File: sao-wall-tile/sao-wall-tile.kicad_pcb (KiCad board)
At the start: 2 copper layers, 100 x 86.5 mm, 22 parts, among them J1 Power In, J2 Power Out, J3 Power Out, J4 Conn_02x03_Odd_Even, J5 Conn_02x03_Odd_Even, J6 Conn_02x03_Odd_Even, J7 Conn_02x03_Odd_Even, U1 LM2594M-3.3

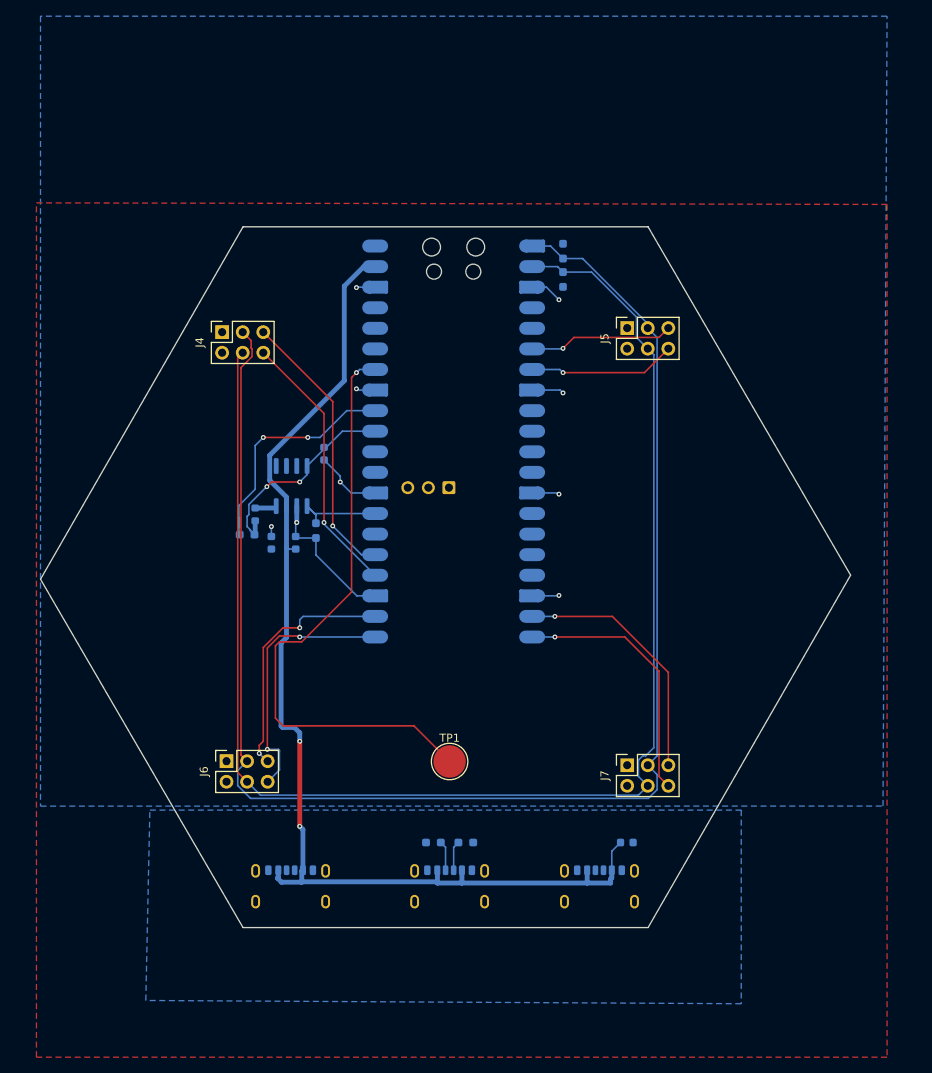
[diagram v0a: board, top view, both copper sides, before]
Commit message: Add README, clean up schematic and layout
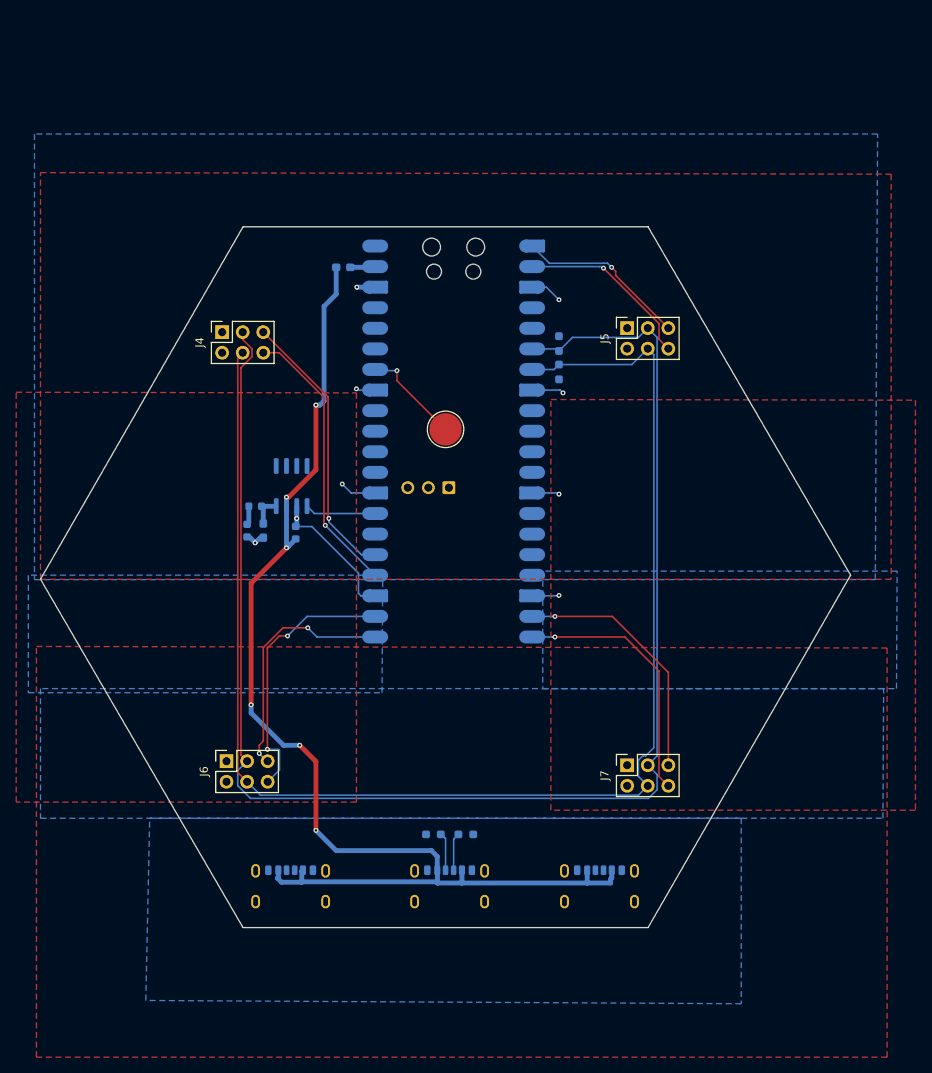
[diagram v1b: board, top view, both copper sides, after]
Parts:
- removed C3: 68uF, Capacitor_SMD:C_0603_1608Metric
- removed C4: 120uF, Capacitor_SMD:C_0603_1608Metric
- removed NT1: NetTie_2, NetTie:NetTie-2_SMD_Pad0.5mm
- removed R1: 1M, Resistor_SMD:R_0603_1608Metric_Pad0.98x0.95mm_HandSolder
- removed R4: 10, Resistor_SMD:R_0603_1608Metric_Pad0.98x0.95mm_HandSolder
- added D1: D_Schottky, Diode_SMD:D_0603_1608Metric_Pad1.05x0.95mm_HandSolder, B.Cu at (102.5, 87.5)
- added D2: D_Schottky, Diode_SMD:D_0603_1608Metric_Pad1.05x0.95mm_HandSolder, B.Cu at (112.4, 55.0)
- C1: value 10uF -> 68uF
- C2: value C -> 120uF
- moved C1 56.0 mm to (106.5, 87.8), turned to 90 degrees
- moved TP1 41.0 mm to (125.0, 75.0)
- moved R2 11.4 mm to (139.0, 64.4)
- moved R3 11.4 mm to (139.0, 67.9)
- moved C2 3.35 mm to (100.5, 87.5), turned to -90 degrees
- moved L1 1.00 mm to (101.5, 84.5), turned to 180 degrees
- moved R7 1.00 mm to (127.5, 125.0)
- moved R8 1.00 mm to (123.5, 125.0)
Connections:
- A1 pad 1: /SAO_SDA -> /SAO2_GPIO1
- A1 pad 2: /SAO_SCL -> /SAO2_GPIO2
- A1 pad 21: /SAO3_GPIO2 -> /SAO3_GPIO1
- A1 pad 22: /SAO3_GPIO1 -> /SAO3_GPIO2
- A1 pad 31: /3V3_HI -> unconnected-(A1-GPIO26_ADC0-Pad31)
- A1 pad 32: /3V3_LO -> unconnected-(A1-GPIO27_ADC1-Pad32)
- A1 pad 39: +5V -> Net-(A1-VSYS)
- A1 pad 6: /SAO2_GPIO1 -> /SAO_SDA
- A1 pad 7: /SAO2_GPIO2 -> /SAO_SCL
- L1 pad 2: /3V3_HI -> +3V3
- U1 pad 4: /3V3_HI -> +3V3
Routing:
- net /TOUCH: track 74.6 -> 12.5 mm
- net /3V3_LO: track 26.4 -> 0.00 mm, vias 2 -> 0
- net /3V3_HI: track 26.1 -> 0.00 mm, vias 2 -> 0
- net +5V: track 139.6 -> 148.8 mm, vias 2 -> 6
- net /SAO_SCL: track 180.0 -> 175.4 mm
- net /SAO2_GPIO2: track 18.2 -> 22.7 mm
- net /SAO2_GPIO1: track 17.9 -> 21.3 mm
- net GND: track 46.8 -> 43.4 mm
- net /SAO_SDA: track 187.9 -> 184.6 mm
- net Net-(A1-VSYS): track 0.00 -> 3.10 mm
- net /EN_3V3: track 11.4 -> 8.78 mm
- net Net-(D1-K): track 2.69 -> 4.03 mm
- net +3V3: track 1.04 -> 2.31 mm
- net /SAO1_GPIO2: track 33.2 -> 34.3 mm
- net Net-(J1-CC2): track 3.71 -> 4.76 mm
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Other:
- board text added: "Power In USB 5V"
- board text added: "Power Out 5V"

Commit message: Update from review feedback
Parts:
- C1, C2: footprint Capacitor_SMD:C_0603_1608Metric -> Capacitor_SMD:C_0805_2012Metric_Pad1.18x1.45mm_HandSolder
- D1, D2: footprint Diode_SMD:D_0603_1608Metric_Pad1.05x0.95mm_HandSolder -> Diode_SMD:D_0805_2012Metric_Pad1.15x1.40mm_HandSolder
- L1: footprint Inductor_SMD:L_0603_1608Metric -> Inductor_SMD:L_0805_2012Metric_Pad1.05x1.20mm_HandSolder
- R2, R3, R7, R8: footprint Resistor_SMD:R_0603_1608Metric_Pad0.98x0.95mm_HandSolder -> Resistor_SMD:R_0805_2012Metric_Pad1.20x1.40mm_HandSolder
- moved D2 1.88 mm to (110.5, 55.0)
- moved R2 1.85 mm to (140.8, 65.0), turned to 180 degrees
- moved R3 1.76 mm to (140.8, 67.8), turned to 180 degrees
- moved C2 1.12 mm to (99.5, 88.0)
- moved C1 1.03 mm to (106.2, 88.8), turned to 0 degrees
- moved A1 1.00 mm to (125.0, 76.5)
- moved R7 0.75 mm to (128.2, 125.0)
- moved R8 0.75 mm to (122.8, 125.0)
- moved D1 0.56 mm to (102.2, 88.0)
- moved L1 0.25 mm to (101.2, 84.5)
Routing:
- net +3V3: track 2.31 -> 191.2 mm, vias 0 -> 1
- net GND: track 43.4 -> 7.90 mm, vias 9 -> 3
- net +5V: track 148.8 -> 137.4 mm, vias 6 -> 0
- net /SAO4_GPIO2: track 32.0 -> 36.3 mm
- net /SAO_SCL: track 175.4 -> 179.7 mm
- net /SAO4_GPIO1: track 31.1 -> 33.9 mm
- net /SAO1_GPIO2: track 34.3 -> 36.1 mm
- net /SAO_SDA: track 184.6 -> 186.1 mm
- net /TOUCH: track 12.5 -> 13.5 mm
- net Net-(A1-VSYS): track 3.10 -> 4.10 mm
- net /EN_3V3: track 8.78 -> 7.78 mm
- net /SAO1_GPIO1: track 34.2 -> 35.1 mm
- net Net-(J1-CC2): track 4.76 -> 5.67 mm
- net Net-(J1-CC1): track 4.71 -> 5.37 mm
- net /SAO2_GPIO2: track 22.7 -> 22.1 mm, vias 1 -> 0
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- removed copper zone on B.Cu, net +3V3
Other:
- board text added: "GPIO1 SDA 3v3 GPIO2 SCL GND"
- board text added: "SAO Wall Tile"
- board text added: "https://github.com/bwasserm/sao-wall v1.0"

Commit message: Updates from picking components on digikey
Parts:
- C1: footprint Capacitor_SMD:C_0805_2012Metric_Pad1.18x1.45mm_HandSolder -> Capacitor_SMD:C_Elec_5x5.8
- C2: footprint Capacitor_SMD:C_0805_2012Metric_Pad1.18x1.45mm_HandSolder -> Capacitor_SMD:C_Elec_8x10.2
- D1: footprint Diode_SMD:D_0805_2012Metric_Pad1.15x1.40mm_HandSolder -> Diode_SMD:D_SOD-123
- L1: value 100uH -> 47uH; footprint Inductor_SMD:L_0805_2012Metric_Pad1.05x1.20mm_HandSolder -> Inductor_SMD:L_Taiyo-Yuden_NR-60xx_HandSoldering
- moved C2 5.37 mm to (95.8, 91.8)
- moved L1 4.37 mm to (99.5, 80.5), turned to 90 degrees
- moved C1 1.68 mm to (107.8, 89.5)
- moved D1 0.50 mm to (101.8, 88.0)
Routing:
- net GND: track 7.90 -> 0.00 mm, vias 3 -> 12
- net Net-(D1-K): track 4.35 -> 9.90 mm
- net +3V3: track 191.2 -> 193.3 mm
- net /SAO1_GPIO1: track 35.1 -> 34.2 mm
- net /SAO1_GPIO2: track 36.1 -> 35.4 mm

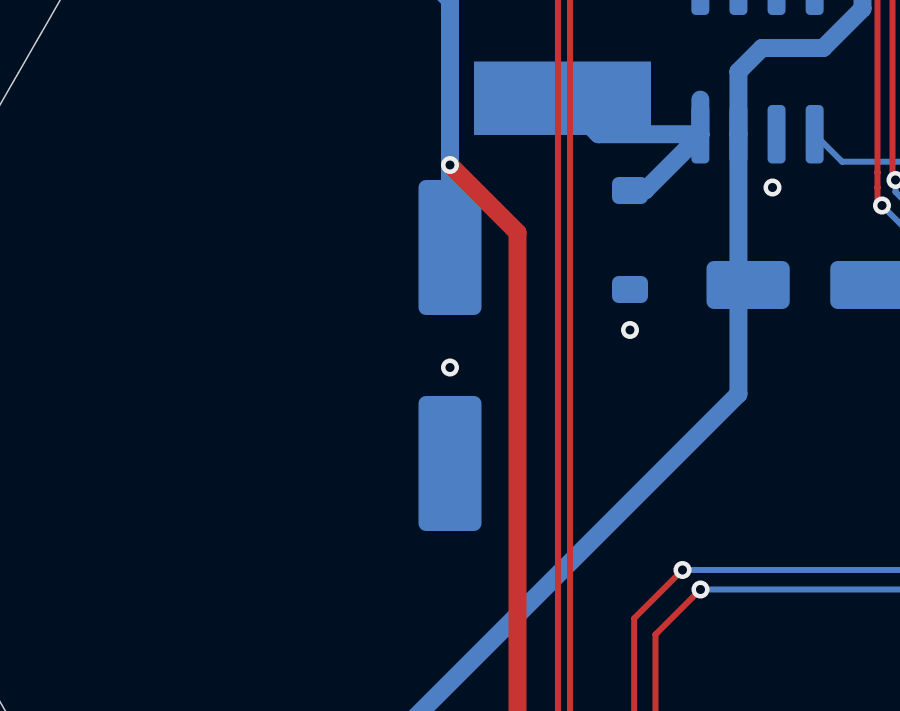
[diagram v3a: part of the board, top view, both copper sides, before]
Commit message: Made C2 smaller
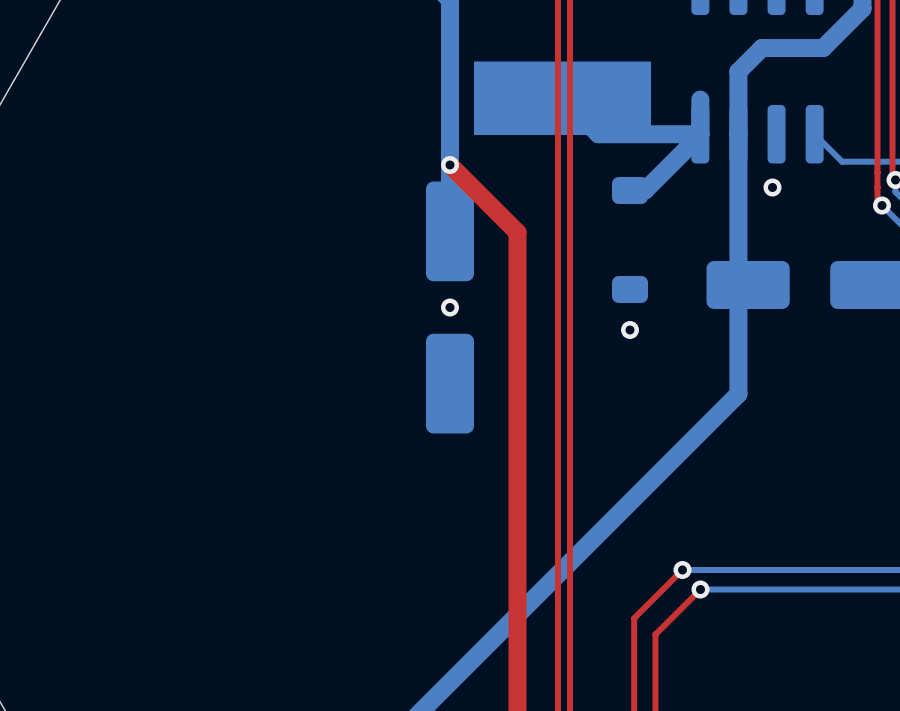
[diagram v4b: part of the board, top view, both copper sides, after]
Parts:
- C2: footprint Capacitor_SMD:C_Elec_8x10.2 -> Capacitor_SMD:C_Elec_6.3x7.7
- moved C2 1.60 mm to (95.8, 90.2)
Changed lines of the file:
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@@
 		)
 	)
-	(footprint "Capacitor_SMD:C_Elec_8x10.2"
+	(footprint "Capacitor_SMD:C_Elec_6.3x7.7"
 		(layer "B.Cu")
-		(at 95.75 91.85 -90)
-		(descr "SMD capacitor, aluminum electrolytic nonpolar, 8.0x10.2mm")
+		(at 95.75 90.25 -90)
+		(descr "SMD capacitor, aluminum electrolytic nonpolar, 6.3x7.7mm")
 		(tags "capacitor electrolyic nonpolar")
 		(property "Reference" "C2"
-			(at 0 5.2 90)
+			(at 0 4.35 90)
 			(layer "B.SilkS")
 			(effects
@@
 		)
 		(property "Value" "120uF"
-			(at 0 -5.2 90)
+			(at 0 -4.35 90)
 			(layer "B.Fab")
 			(effects
@@
 		(attr smd)
 		(fp_line
-			(start -3.195563 4.26)
-			(end 4.26 4.26)
+			(start -2.345563 3.41)
+			(end 3.41 3.41)
 			(stroke
 				(width 0.12)
@@
 		)
 		(fp_line
-			(start 4.26 4.26)
-			(end 4.26 1.31)
+			(start 3.41 3.41)
+			(end 3.41 1.06)
 			(stroke
 				(width 0.12)
@@
 		)
 		(fp_line
-			(start -4.26 3.195563)
-			(end -3.195563 4.26)
+			(start -3.41 2.345563)
+			(end -2.345563 3.41)
 			(stroke
 				(width 0.12)
@@
 		)
 		(fp_line
-			(start -4.26 3.195563)
-			(end -4.26 1.31)
+			(start -3.41 2.345563)
+			(end -3.41 1.06)
 			(stroke
 				(width 0.12)
@@
 		)
 		(fp_line
-			(start -4.26 -3.195563)
-			(end -4.26 -1.31)
+			(start -3.41 -2.345563)
+			(end -3.41 -1.06)
 			(stroke
 				(width 0.12)
@@
 		)
 		(fp_line
-			(start -4.26 -3.195563)
-			(end -3.195563 -4.26)
+			(start -3.41 -2.345563)
+			(end -2.345563 -3.41)
 			(stroke
 				(width 0.12)
@@
 		)
 		(fp_line
-			(start -3.195563 -4.26)
-			(end 4.26 -4.26)
+			(start -2.345563 -3.41)
+			(end 3.41 -3.41)
 			(stroke
 				(width 0.12)
@@
 		)
 		(fp_line
-			(start 4.26 -4.26)
-			(end 4.26 -1.31)
+			(start 3.41 -3.41)
+			(end 3.41 -1.06)
 			(stroke
 				(width 0.12)
@@
 		)
 		(fp_line
-			(start -3.25 4.4)
-			(end 4.4 4.4)
+			(start -2.4 3.55)
+			(end 3.55 3.55)
 			(stroke
 				(width 0.05)
@@
 		)
 		(fp_line
-			(start 4.4 4.4)
-			(end 4.4 1.3)
+			(start 3.55 3.55)
+			(end 3.55 1.05)
 			(stroke
 				(width 0.05)
@@
 		)
 		(fp_line
-			(start -4.4 3.25)
-			(end -3.25 4.4)
+			(start -3.55 2.4)
+			(end -2.4 3.55)
 			(stroke
 				(width 0.05)
@@
 		)
 		(fp_line
-			(start -4.4 3.25)
-			(end -4.4 1.3)
+			(start -3.55 2.4)
+			(end -3.55 1.05)
 			(stroke
 				(width 0.05)
@@
 		)
 		(fp_line
-			(start -6.1 1.3)
-			(end -6.1 -1.3)
+			(start -4.45 1.05)
+			(end -4.45 -1.05)
 			(stroke
 				(width 0.05)
@@
 		)
 		(fp_line
-			(start -4.4 1.3)
-			(end -6.1 1.3)
+			(start -3.55 1.05)
+			(end -4.45 1.05)
 			(stroke
 				(width 0.05)
@@
 		)
 		(fp_line
-			(start 4.4 1.3)
-			(end 6.1 1.3)
+			(start 3.55 1.05)
+			(end 4.45 1.05)
 			(stroke
 				(width 0.05)
@@
 		)
 		(fp_line
-			(start 6.1 1.3)
-			(end 6.1 -1.3)
+			(start 4.45 1.05)
+			(end 4.45 -1.05)
 			(stroke
 				(width 0.05)
@@
 		)
 		(fp_line
-			(start -6.1 -1.3)
-			(end -4.4 -1.3)
+			(start -4.45 -1.05)
+			(end -3.55 -1.05)
 			(stroke
 				(width 0.05)
@@
 		)
 		(fp_line
-			(start -4.4 -1.3)
-			(end -4.4 -3.25)
+			(start -3.55 -1.05)
+			(end -3.55 -2.4)
 			(stroke
 				(width 0.05)
@@
 		)
 		(fp_line
-			(start 4.4 -1.3)
-			(end 4.4 -4.4)
+			(start 3.55 -1.05)
+			(end 3.55 -3.55)
 			(stroke
 				(width 0.05)
@@
 		)
 		(fp_line
-			(start 6.1 -1.3)
-			(end 4.4 -1.3)
+			(start 4.45 -1.05)
+			(end 3.55 -1.05)
 			(stroke
 				(width 0.05)
@@
 		)
 		(fp_line
-			(start -4.4 -3.25)
-			(end -3.25 -4.4)
+			(start -3.55 -2.4)
+			(end -2.4 -3.55)
 			(stroke
 				(width 0.05)
@@
 		)
 		(fp_line
-			(start -3.25 -4.4)
-			(end 4.4 -4.4)
+			(start -2.4 -3.55)
+			(end 3.55 -3.55)
 			(stroke
 				(width 0.05)
@@
 		)
 		(fp_line
-			(start -3.15 4.15)
-			(end 4.15 4.15)
+			(start -2.3 3.3)
+			(end 3.3 3.3)
 			(stroke
 				(width 0.1)
@@
 		)
 		(fp_line
-			(start 4.15 4.15)
-			(end 4.15 -4.15)
+			(start 3.3 3.3)
+			(end 3.3 -3.3)
 			(stroke
 				(width 0.1)
@@
 		)
 		(fp_line
-			(start -4.15 3.15)
-			(end -3.15 4.15)
+			(start -3.3 2.3)
+			(end -2.3 3.3)
 			(stroke
 				(width 0.1)
@@
 		)
 		(fp_line
-			(start -4.15 3.15)
-			(end -4.15 -3.15)
+			(start -3.3 2.3)
+			(end -3.3 -2.3)
 			(stroke
 				(width 0.1)
@@
 		)
 		(fp_line
-			(start -4.15 -3.15)
-			(end -3.15 -4.15)
+			(start -3.3 -2.3)
+			(end -2.3 -3.3)
 			(stroke
 				(width 0.1)
@@
 		)
 		(fp_line
-			(start -3.15 -4.15)
-			(end 4.15 -4.15)
+			(start -2.3 -3.3)
+			(end 3.3 -3.3)
 			(stroke
 				(width 0.1)
@@
 		(fp_circle
 			(center 0 0)
-			(end 4 0)
+			(end 3.15 0)
 			(stroke
 				(width 0.1)
@@
 		)
 		(pad "1" smd roundrect
-			(at -3.6 0 270)
-			(size 4.5 2.1)
+			(at -2.5375 0 270)
+			(size 3.325 1.6)
 			(layers "B.Cu" "B.Mask" "B.Paste")
-			(roundrect_rratio 0.119048)
+			(roundrect_rratio 0.15625)
 			(net 16 "+3V3")
 			(pintype "passive")
 		)
 		(pad "2" smd roundrect
-			(at 3.6 0 270)
-			(size 4.5 2.1)
+			(at 2.5375 0 270)
+			(size 3.325 1.6)
 			(layers "B.Cu" "B.Mask" "B.Paste")
-			(roundrect_rratio 0.119048)
+			(roundrect_rratio 0.15625)
 			(net 3 "GND")
 			(pintype "passive")
 		)
 		(embedded_fonts no)
-		(model "${KICAD9_3DMODEL_DIR}/Capacitor_SMD.3dshapes/C_Elec_8x10.2.wrl"
+		(model "${KICAD9_3DMODEL_DIR}/Capacitor_SMD.3dshapes/C_Elec_6.3x7.7.wrl"
 			(offset
 				(xyz 0 0 0)
@@
 	)
 	(via
-		(at 95.75 92.25)
+		(at 95.75 90.25)
 		(size 0.6)
 		(drill 0.3)

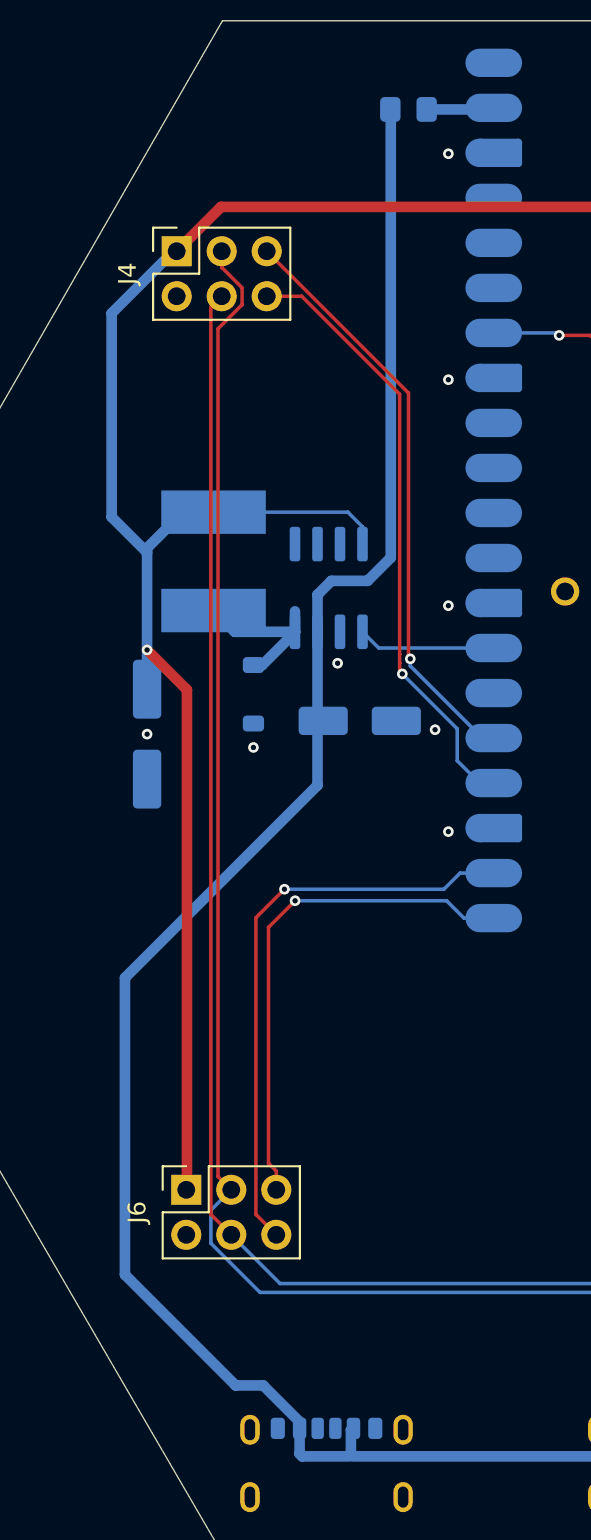
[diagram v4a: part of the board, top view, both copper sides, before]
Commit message: Different buck converter for smaller and cheaper components
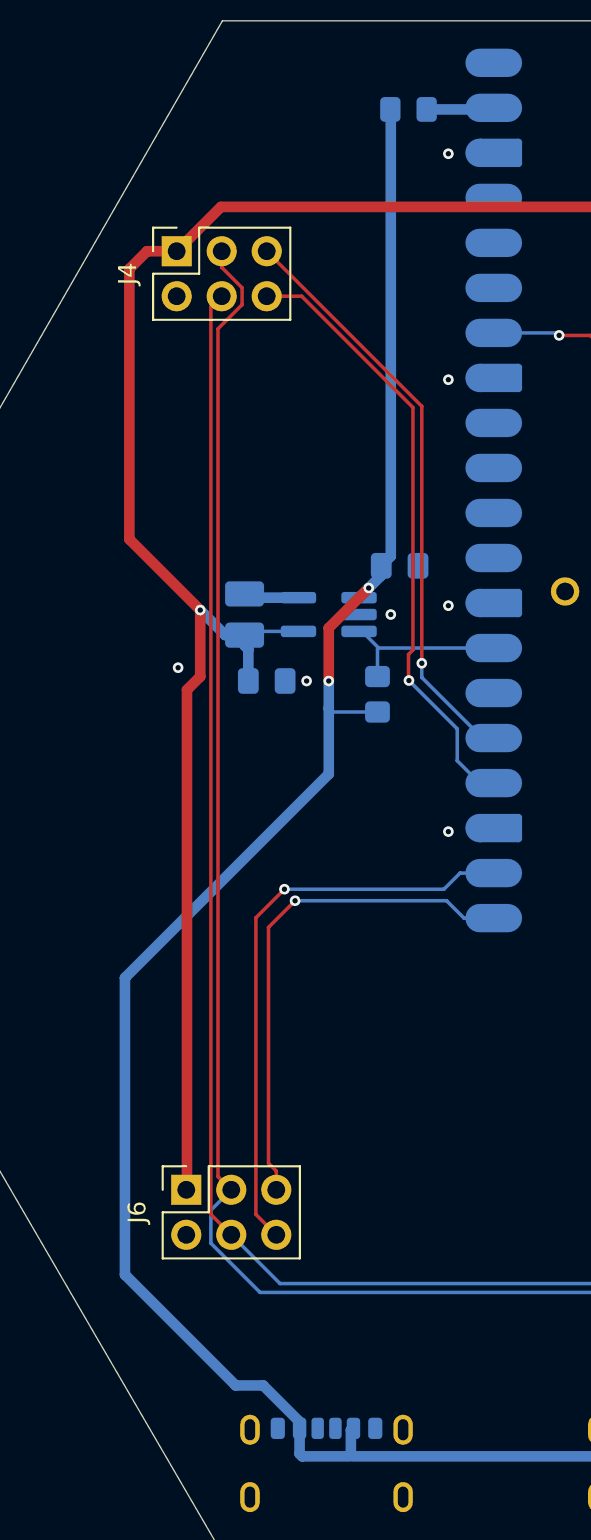
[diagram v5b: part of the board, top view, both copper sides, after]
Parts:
- removed D1: D_Schottky, Diode_SMD:D_SOD-123
- added R1: 1M, Resistor_SMD:R_0805_2012Metric_Pad1.20x1.40mm_HandSolder, B.Cu at (108.8, 88.0)
- C1: value 68uF -> 4.7uF; footprint Capacitor_SMD:C_Elec_5x5.8 -> Capacitor_SMD:C_0805_2012Metric_Pad1.18x1.45mm_HandSolder
- C2: value 120uF -> 4.7uF; footprint Capacitor_SMD:C_Elec_6.3x7.7 -> Capacitor_SMD:C_0805_2012Metric_Pad1.18x1.45mm_HandSolder
- L1: value 47uH -> 4.7uH; footprint Inductor_SMD:L_Taiyo-Yuden_NR-60xx_HandSoldering -> Inductor_SMD:L_1008_2520Metric_Pad1.43x2.20mm_HandSolder
- U1: value LM2594M-3.3 -> ~; footprint Package_SO:SOIC-8_3.9x4.9mm_P1.27mm -> Package_TO_SOT_SMD:TSOT-23-5_HandSoldering
- moved C1 9.03 mm to (110.0, 80.8)
- moved C2 7.39 mm to (102.5, 87.2), turned to 0 degrees
- moved L1 3.47 mm to (101.2, 83.5), turned to -90 degrees
- moved U1 1.50 mm to (106.0, 83.5), turned to 180 degrees
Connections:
- L1 pad 1: Net-(D1-K) -> Net-(U1-Lx)
- U1 pad 1: unconnected-(U1-NC-Pad1) -> +5V
- U1 pad 2: unconnected-(U1-NC-Pad2) -> GND
- U1 pad 3: unconnected-(U1-NC-Pad3) -> /EN_3V3
- U1 pad 5: /EN_3V3 -> Net-(U1-Lx)
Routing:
- net Net-(D1-K): track 9.90 -> 0.00 mm
- net +3V3: track 193.3 -> 185.7 mm
- net Net-(U1-Lx): track 0.00 -> 3.13 mm
- net +5V: track 137.4 -> 139.8 mm, vias 0 -> 2
- net /EN_3V3: track 7.78 -> 9.42 mm
- net GND: vias 12 -> 11
